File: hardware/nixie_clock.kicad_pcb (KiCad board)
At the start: 2 copper layers, 224 x 70 mm, 100 parts, among them J1 Conn_02x02_Odd_Even, J2 USB_C_Receptacle_USB2.0_16P, J7 Barrel_Jack_Switch, Q1 IRF740, Q2 BSS138, Q3 BSS138, Q4 BSS138, Q5 BSS138, Q6 BSS138, Q7 BSS138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

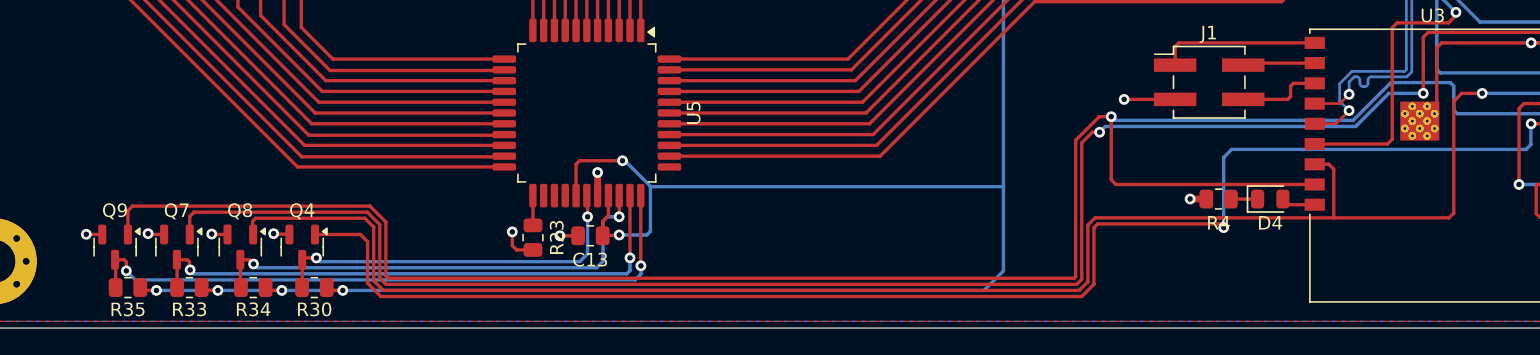
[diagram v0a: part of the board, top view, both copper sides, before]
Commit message: Remove one mosfet on the right since SPI out from the first HV5622 is already on 12v level.
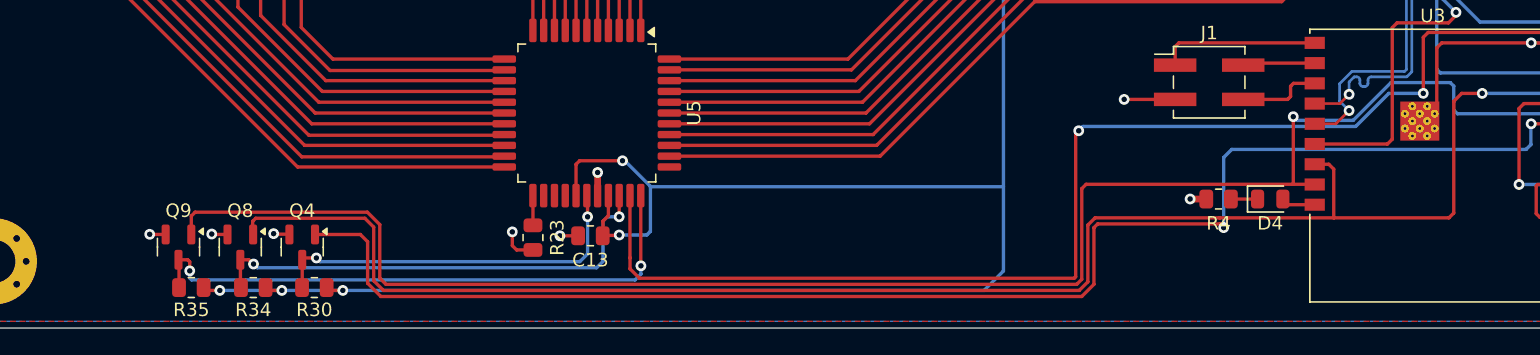
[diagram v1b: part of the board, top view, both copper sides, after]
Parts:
- removed Q7: BSS138, Package_TO_SOT_SMD:SOT-23
- removed R33: 10k, Resistor_SMD:R_0805_2012Metric
- moved Q9 4.70 mm to (68.7, 124.0)
- moved R35 4.70 mm to (69.6, 127.0)
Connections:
- U5 pad 32: Net-(Q7-D) -> /driver_3_digits_1_dot_left/SPI_SDO
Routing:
- net Net-(Q7-D): track 42.1 -> 0.00 mm, vias 2 -> 0
- net /driver_3_digits_1_dot_left/SPI_SDO: track 196.7 -> 163.8 mm
- net /cpu/GPIO1: track 246.2 -> 223.4 mm
- net /connectors/12V: track 462.0 -> 456.4 mm, vias 15 -> 14
- net Net-(Q9-D): track 48.1 -> 43.7 mm
- net /connectors/GND: track 135.9 -> 134.6 mm, vias 34 -> 33

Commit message: Tweaks.
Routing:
- net /connectors/12V: track 456.4 -> 427.4 mm
- net /connectors/GND: track 134.6 -> 133.8 mm

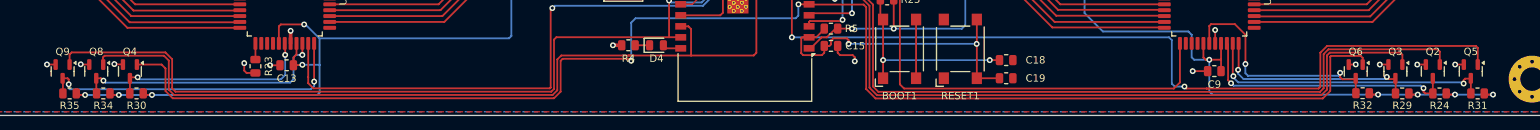
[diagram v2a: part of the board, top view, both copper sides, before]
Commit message: Making tracks to mosfets shorter.
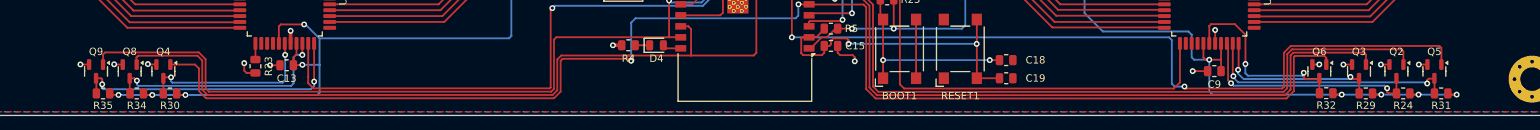
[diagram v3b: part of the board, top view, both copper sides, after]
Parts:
- moved Q2 4.96 mm to (250.5, 124.0)
- moved Q3 4.96 mm to (245.4, 124.0)
- moved Q6 4.96 mm to (240.0, 124.0)
- moved R29 4.96 mm to (246.3, 127.0)
- moved R32 4.96 mm to (240.9, 127.0)
- moved Q5 4.96 mm to (255.7, 124.0)
- moved R24 4.96 mm to (251.4, 127.0)
- moved R31 4.96 mm to (256.6, 127.0)
- moved Q4 4.56 mm to (82.4, 124.0)
- moved Q8 4.56 mm to (77.8, 124.0)
- moved Q9 4.56 mm to (73.3, 124.0)
- moved R30 4.56 mm to (83.3, 127.0)
- moved R34 4.56 mm to (78.8, 127.0)
- moved R35 4.56 mm to (74.2, 127.0)
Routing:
- net /cpu/SPI_CLK: track 200.9 -> 191.3 mm
- net /cpu/GPIO2: track 225.8 -> 216.3 mm
- net /cpu/GPIO1: track 223.4 -> 213.9 mm
- net Net-(Q6-D): track 31.4 -> 26.4 mm
- net Net-(Q5-D): track 40.0 -> 35.0 mm
- net Net-(Q3-D): track 28.2 -> 23.2 mm
- net Net-(Q2-D): track 36.1 -> 31.1 mm
- net /connectors/12V: track 427.4 -> 422.4 mm
- net /cpu/SPI_MOSI: track 115.6 -> 110.6 mm
- net Net-(Q9-D): track 43.7 -> 39.1 mm
- net Net-(Q8-D): track 35.4 -> 31.8 mm
- net Net-(Q4-D): track 28.1 -> 24.7 mm

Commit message: Update.
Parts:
- moved Q8 0.70 mm to (78.5, 124.0)
- moved Q9 0.70 mm to (74.0, 124.0)
- moved R30 0.70 mm to (84.0, 127.0)
- moved R34 0.70 mm to (79.5, 127.0)
- moved R35 0.70 mm to (74.9, 127.0)
- moved Q4 0.70 mm to (83.1, 124.0)
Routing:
- net /cpu/GPIO2: track 216.3 -> 215.6 mm
- net /cpu/GPIO1: track 213.9 -> 213.2 mm
- net Net-(Q9-D): track 39.1 -> 38.4 mm
- net Net-(Q4-D): track 24.7 -> 24.0 mm
- net Net-(Q8-D): track 31.8 -> 31.1 mm
- net /cpu/SPI_CLK: track 191.3 -> 190.6 mm

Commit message: Remove one via near HV5622. Tweaks.
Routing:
- net /connectors/GND: track 133.8 -> 131.1 mm, vias 33 -> 32
- net /connectors/12V: track 422.4 -> 423.6 mm
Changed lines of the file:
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@@
 	)
 	(segment
-		(start 191.7402 117.7198)
+		(start 191.7402 117.8098)
 		(end 191.7402 79.17)
 		(width 0.25)
@@
 	)
 	(segment
-		(start 176.305 118.17)
-		(end 176.3 118.165)
+		(start 181.984 118.17)
+		(end 191.38 118.17)
 		(width 0.25)
 		(layer "B.Cu")
@@
 	)
 	(segment
-		(start 181.984 118.17)
-		(end 191.29 118.17)
+		(start 191.38 118.17)
+		(end 191.7402 117.8098)
 		(width 0.25)
 		(layer "B.Cu")
@@
 	)
 	(segment
-		(start 181.984 118.17)
-		(end 176.305 118.17)
+		(start 176.305 118.17)
+		(end 176.3 118.165)
 		(width 0.25)
 		(layer "B.Cu")
@@
 	)
 	(segment
-		(start 191.29 118.17)
-		(end 191.7402 117.7198)
+		(start 181.984 118.17)
+		(end 176.305 118.17)
 		(width 0.25)
 		(layer "B.Cu")
@@
 	)
 	(segment
-		(start 207.3977 61.5275)
-		(end 207.9852 62.115)
+		(start 129.87 119.135)
+		(end 129.87 72.38)
 		(width 0.25)
 		(layer "B.Cu")
@@
 	)
 	(segment
-		(start 96.04 61.5275)
-		(end 207.4075 61.5275)
+		(start 207.3977 61.5275)
+		(end 207.9852 62.115)
 		(width 0.25)
 		(layer "B.Cu")
@@
 	)
 	(segment
-		(start 129.55 119.49)
-		(end 129.87 119.17)
+		(start 96.04 61.5275)
+		(end 207.4075 61.5275)
 		(width 0.25)
 		(layer "B.Cu")
@@
 	)
 	(segment
-		(start 103.69 119.49)
-		(end 129.55 119.49)
-		(width 0.25)
-		(layer "B.Cu")
-		(net 12)
-	)
-	(segment
 		(start 225.46 127.16)
 		(end 243.05 127.16)
@@
 	)
 	(segment
-		(start 103.72 126.9)
-		(end 103.72 123.11)
+		(start 207.995 76.035033)
+		(end 207.995 118.2025)
 		(width 0.25)
 		(layer "B.Cu")
@@
 	)
 	(segment
-		(start 207.995 116.05)
-		(end 210.5 118.555)
+		(start 103.72 126.9)
+		(end 103.72 123.11)
 		(width 0.25)
 		(layer "B.Cu")
@@
 	)
 	(segment
-		(start 222.15 118.555)
-		(end 222.6 119.005)
+		(start 208.3475 118.555)
+		(end 222.15 118.555)
 		(width 0.25)
 		(layer "B.Cu")
@@
 	)
 	(segment
-		(start 129.87 119.17)
-		(end 129.87 72.38)
+		(start 101.62 117.595)
+		(end 101.795 117.595)
 		(width 0.25)
 		(layer "B.Cu")
@@
 	)
 	(segment
-		(start 222.6 122.075)
-		(end 222.93 122.405)
+		(start 96.039792 61.527708)
+		(end 96.04 61.5275)
 		(width 0.25)
 		(layer "B.Cu")
@@
 	)
 	(segment
-		(start 96.039792 61.527708)
-		(end 96.04 61.5275)
+		(start 88.6575 61.5275)
+		(end 88.399792 61.785208)
 		(width 0.25)
 		(layer "B.Cu")
@@
 	)
 	(segment
-		(start 88.6575 61.5275)
-		(end 88.399792 61.785208)
+		(start 101.795 117.595)
+		(end 103.69 119.49)
 		(width 0.25)
 		(layer "B.Cu")
@@
 	)
 	(segment
-		(start 210.5 118.555)
-		(end 222.15 118.555)
+		(start 129.515 119.49)
+		(end 129.87 119.135)
 		(width 0.25)
 		(layer "B.Cu")
@@
 	)
 	(segment
-		(start 101.795 117.595)
-		(end 103.69 119.49)
+		(start 103.69 119.49)
+		(end 129.515 119.49)
 		(width 0.25)
 		(layer "B.Cu")
@@
 	)
 	(segment
+		(start 222.6 122.075)
+		(end 222.93 122.405)
+		(width 0.25)
+		(layer "B.Cu")
+		(net 12)
+	)
+	(segment
 		(start 101.375 123.1)
 		(end 103.71 123.1)
@@
 	)
 	(segment
-		(start 222.6 119.005)
-		(end 222.6 122.075)
+		(start 222.15 118.555)
+		(end 222.6 119.005)
 		(width 0.25)
 		(layer "B.Cu")
@@
 	)
 	(segment
-		(start 258.72 127.16)
-		(end 253.52 127.16)
+		(start 222.93 122.405)
+		(end 225 122.405)
 		(width 0.25)
 		(layer "B.Cu")
@@
 	)
 	(segment
-		(start 222.93 122.405)
-		(end 225 122.405)
+		(start 207.995 118.2025)
+		(end 208.3475 118.555)
 		(width 0.25)
 		(layer "B.Cu")
@@
 	)
 	(segment
-		(start 207.9852 62.115)
-		(end 207.9852 76.035033)
+		(start 258.72 127.16)
+		(end 253.52 127.16)
 		(width 0.25)
 		(layer "B.Cu")
@@
 	)
 	(segment
-		(start 101.62 117.595)
-		(end 101.795 117.595)
+		(start 207.9852 62.115)
+		(end 207.9852 76.035033)
 		(width 0.25)
 		(layer "B.Cu")
@@
 	)
 	(segment
-		(start 207.995 76.035033)
-		(end 207.995 116.05)
+		(start 222.6 119.005)
+		(end 222.6 122.075)
 		(width 0.25)
 		(layer "B.Cu")
@@
 	)
 	(segment
-		(start 93.45 122.87)
-		(end 93.45 123.89)
-		(width 0.25)
-		(layer "F.Cu")
-		(net 122)
-	)
-	(segment
 		(start 97.669792 71.0075)
 		(end 96.072292 71.0075)
@@
 	)
 	(segment
-		(start 93.45 123.89)
-		(end 93.7675 124.2075)
-		(width 0.25)
-		(layer "F.Cu")
-		(net 122)
-	)
-	(segment
 		(start 126.27 73.75)
 		(end 126.28 73.74)
@@
 	)
 	(segment
-		(start 93.7675 124.2075)
-		(end 94.98 124.2075)
-		(width 0.25)
-		(layer "F.Cu")
-		(net 122)
-	)
-	(segment
 		(start 198.324 122.3625)
 		(end 198.2265 122.46)
@@
 		(size 0.8)
 		(drill 0.4)
-		(layers "F.Cu" "B.Cu")
-		(net 122)
-	)
-	(via
-		(at 93.45 122.87)
-		(size 0.8)
-		(drill 0.4)

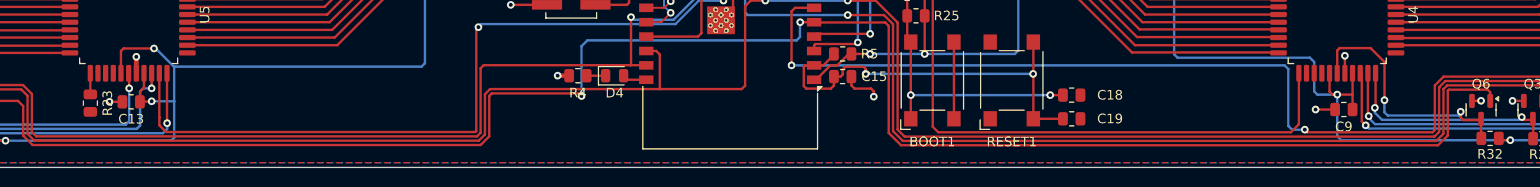
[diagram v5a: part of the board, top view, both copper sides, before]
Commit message: Remove one unused track.
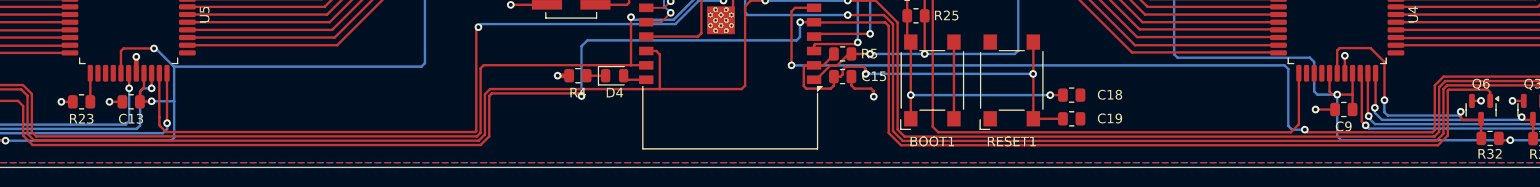
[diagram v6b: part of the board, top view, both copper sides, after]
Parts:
- moved R23 0.92 mm to (94.1, 123.2), turned to 180 degrees
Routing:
- net /connectors/GND: track 131.1 -> 132.3 mm, vias 32 -> 33
- net Net-(U5A-DATA_OUT): track 2.20 -> 2.98 mm
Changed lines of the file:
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@@
 	(footprint "Resistor_SMD:R_0805_2012Metric"
 		(layer "F.Cu")
-		(at 94.98 123.295 -90)
+		(at 94.07 123.16 180)
 		(descr "Resistor SMD 0805 (2012 Metric), square (rectangular) end terminal, IPC-7351 nominal, (Body size source: IPC-SM-782 page 72, https://www.pcb-3d.com/wordpress/wp-content/uploads/ipc-sm-782a_amendment_1_and_2.pdf), generated with kicad-footprint-generator")
 		(tags "resistor")
 		(property "Reference" "R23"
-			(at 0 -1.8 90)
+			(at 0 -1.8 0)
 			(layer "F.SilkS")
 			(effects
@@
 		)
 		(property "Value" "10K"
-			(at 0 2.42 90)
+			(at 0 2.42 0)
 			(layer "F.Fab")
 			(effects
@@
 		)
 		(property "Datasheet" ""
-			(at 0 0 90)
+			(at 0 0 0)
 			(layer "F.Fab")
 			(hide yes)
@@
 		)
 		(property "Description" "Resistor"
-			(at 0 0 90)
+			(at 0 0 0)
 			(layer "F.Fab")
 			(hide yes)
@@
 		)
 		(fp_line
-			(start -1.68 0.95)
-			(end -1.68 -0.95)
+			(start 1.68 0.95)
+			(end -1.68 0.95)
 			(stroke
 				(width 0.05)
@@
 		)
 		(fp_line
-			(start 1.68 0.95)
-			(end -1.68 0.95)
+			(start 1.68 -0.95)
+			(end 1.68 0.95)
 			(stroke
 				(width 0.05)
@@
 		)
 		(fp_line
-			(start -1.68 -0.95)
-			(end 1.68 -0.95)
+			(start -1.68 0.95)
+			(end -1.68 -0.95)
 			(stroke
 				(width 0.05)
@@
 		)
 		(fp_line
-			(start 1.68 -0.95)
-			(end 1.68 0.95)
+			(start -1.68 -0.95)
+			(end 1.68 -0.95)
 			(stroke
 				(width 0.05)
@@
 		)
 		(fp_line
-			(start -1 0.625)
-			(end -1 -0.625)
+			(start 1 0.625)
+			(end -1 0.625)
 			(stroke
 				(width 0.1)
@@
 		)
 		(fp_line
-			(start 1 0.625)
-			(end -1 0.625)
+			(start 1 -0.625)
+			(end 1 0.625)
 			(stroke
 				(width 0.1)
@@
 		)
 		(fp_line
-			(start -1 -0.625)
-			(end 1 -0.625)
+			(start -1 0.625)
+			(end -1 -0.625)
 			(stroke
 				(width 0.1)
@@
 		)
 		(fp_line
-			(start 1 -0.625)
-			(end 1 0.625)
+			(start -1 -0.625)
+			(end 1 -0.625)
 			(stroke
 				(width 0.1)
@@
 		)
 		(fp_text user "${REFERENCE}"
-			(at 0 0 90)
+			(at 0 0 0)
 			(layer "F.Fab")
 			(effects
@@
 		)
 		(pad "1" smd roundrect
-			(at -0.9125 0 270)
+			(at -0.9125 0 180)
 			(size 1.025 1.4)
 			(layers "F.Cu" "F.Mask" "F.Paste")
@@
 		)
 		(pad "2" smd roundrect
-			(at 0.9125 0 270)
+			(at 0.9125 0 180)
 			(size 1.025 1.4)
 			(layers "F.Cu" "F.Mask" "F.Paste")
@@
 	)
 	(segment
-		(start 94.98 120.185)
-		(end 94.975 120.18)
+		(start 94.9825 123.16)
+		(end 94.9825 120.1875)
 		(width 0.25)
 		(layer "F.Cu")
@@
 	)
 	(segment
-		(start 94.98 122.3825)
-		(end 94.98 120.185)
+		(start 94.9825 120.1875)
+		(end 94.975 120.18)
 		(width 0.25)
 		(layer "F.Cu")
@@
 	)
 	(segment
+		(start 93.1575 123.16)
+		(end 91.94 123.16)
+		(width 0.25)
+		(layer "F.Cu")
+		(net 122)
+	)
+	(segment
 		(start 96.069792 71.01)
 		(end 96.072292 71.0075)
@@
 	)
 	(segment
-		(start 240.02 123.05)
-		(end 240.01 123.06)
-		(width 0.25)
-		(layer "F.Cu")
-		(net 122)
-	)
-	(segment
 		(start 249.56 123.0625)
 		(end 248.45 123.0625)
@@
 		(size 0.8)
 		(drill 0.4)
+		(layers "F.Cu" "B.Cu")
+		(net 122)
+	)
+	(via
+		(at 91.96 123.16)
+		(size 0.8)
+		(drill 0.4)

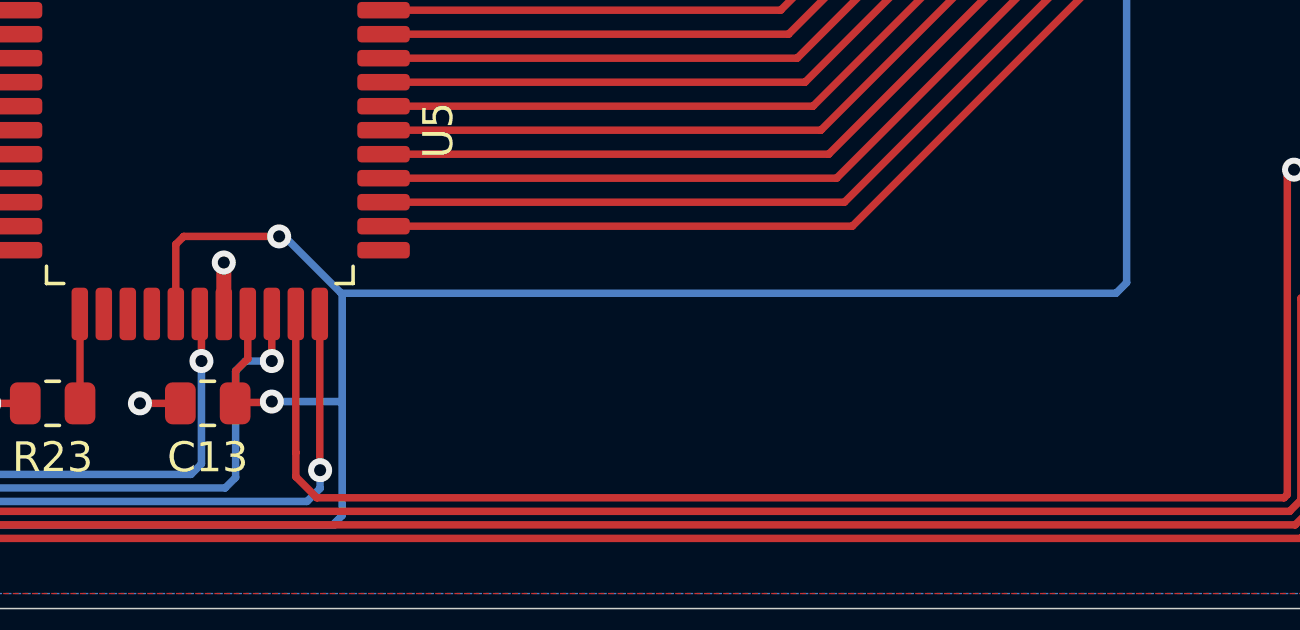
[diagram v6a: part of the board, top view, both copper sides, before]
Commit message: Simplify 12V rail on U5.
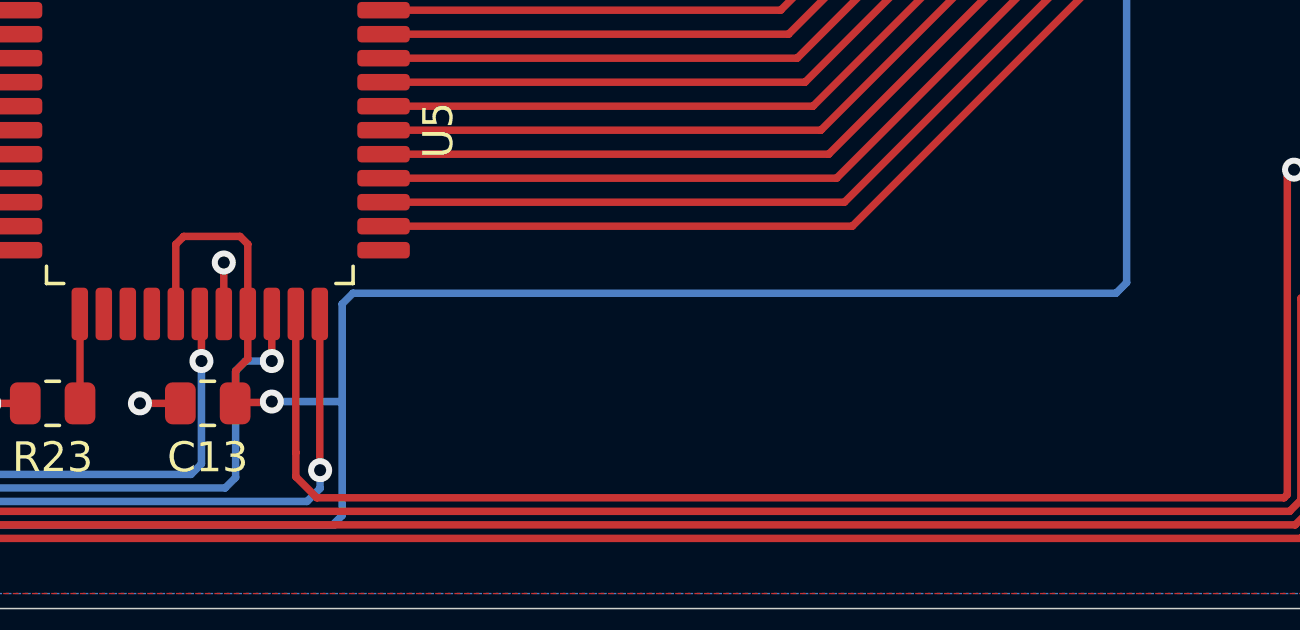
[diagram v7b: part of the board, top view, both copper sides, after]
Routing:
- net /connectors/12V: track 423.6 -> 422.0 mm, vias 14 -> 13
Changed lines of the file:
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@@
 	)
 	(segment
+		(start 100.315 117.595)
+		(end 98.44 117.595)
+		(width 0.25)
+		(layer "F.Cu")
+		(net 12)
+	)
+	(segment
+		(start 100.575 120.18)
+		(end 100.575 117.855)
+		(width 0.25)
+		(layer "F.Cu")
+		(net 12)
+	)
+	(segment
 		(start 81.62 127.21)
 		(end 80.5525 127.21)
@@
 	)
 	(segment
-		(start 131.1375 74.01)
-		(end 130.15 74.01)
+		(start 98.44 117.595)
+		(end 98.175 117.86)
 		(width 0.25)
 		(layer "F.Cu")
@@
 	)
 	(segment
-		(start 101.62 117.595)
-		(end 98.44 117.595)
+		(start 131.1375 74.01)
+		(end 130.15 74.01)
 		(width 0.25)
 		(layer "F.Cu")
@@
 	)
 	(segment
-		(start 98.175 117.86)
-		(end 98.175 120.18)
+		(start 224.505 122.405)
+		(end 224.2 122.1)
 		(width 0.25)
 		(layer "F.Cu")
@@
 	)
 	(segment
-		(start 224.505 122.405)
-		(end 224.2 122.1)
+		(start 226.6025 120.1825)
+		(end 226.6 120.18)
 		(width 0.25)
 		(layer "F.Cu")
@@
 	)
 	(segment
-		(start 226.6025 120.1825)
-		(end 226.6 120.18)
+		(start 100.575 117.855)
+		(end 100.315 117.595)
 		(width 0.25)
 		(layer "F.Cu")
@@
 	)
 	(segment
-		(start 98.44 117.595)
-		(end 98.175 117.86)
-		(width 0.25)
-		(layer "F.Cu")
-		(net 12)
-	)
-	(segment
 		(start 226.6025 123.84)
 		(end 226.6025 122.4)
@@
 	)
 	(segment
+		(start 98.175 117.86)
+		(end 98.175 120.18)
+		(width 0.25)
+		(layer "F.Cu")
+		(net 12)
+	)
+	(segment
 		(start 257.6825 127.16)
 		(end 257.5225 127)
@@
 	)
 	(via
-		(at 101.62 117.595)
-		(size 0.8)
-		(drill 0.4)
-		(layers "F.Cu" "B.Cu")
-		(net 12)
-	)
-	(via
 		(at 225 122.405)
 		(size 0.8)
@@
 	)
 	(segment
-		(start 129.87 119.135)
-		(end 129.87 72.38)
-		(width 0.25)
-		(layer "B.Cu")
-		(net 12)
-	)
-	(segment
 		(start 207.3977 61.5275)
 		(end 207.9852 62.115)
@@
 	)
 	(segment
-		(start 96.04 61.5275)
-		(end 207.4075 61.5275)
+		(start 104.08 119.49)
+		(end 129.515 119.49)
 		(width 0.25)
 		(layer "B.Cu")
@@
 	)
 	(segment
-		(start 103.72 123.11)
-		(end 103.72 119.55)
+		(start 96.04 61.5275)
+		(end 207.4075 61.5275)
 		(width 0.25)
 		(layer "B.Cu")
@@
 	)
 	(segment
+		(start 129.515 119.49)
+		(end 129.87 119.135)
+		(width 0.25)
+		(layer "B.Cu")
+		(net 12)
+	)
+	(segment
 		(start 103.72 126.9)
 		(end 103.72 123.11)
@@
 	)
 	(segment
+		(start 129.87 119.135)
+		(end 129.87 72.38)
+		(width 0.25)
+		(layer "B.Cu")
+		(net 12)
+	)
+	(segment
 		(start 208.3475 118.555)
 		(end 222.15 118.555)
@@
 	)
 	(segment
-		(start 101.62 117.595)
-		(end 101.795 117.595)
-		(width 0.25)
-		(layer "B.Cu")
-		(net 12)
-	)
-	(segment
 		(start 96.039792 61.527708)
 		(end 96.04 61.5275)
@@
 	)
 	(segment
-		(start 101.795 117.595)
-		(end 103.69 119.49)
+		(start 103.72 123.11)
+		(end 103.72 119.85)
 		(width 0.25)
 		(layer "B.Cu")
@@
 	)
 	(segment
-		(start 129.515 119.49)
-		(end 129.87 119.135)
-		(width 0.25)
-		(layer "B.Cu")
-		(net 12)
-	)
-	(segment
 		(start 225 126.74)
 		(end 225.42 127.16)
@@
 	)
 	(segment
-		(start 103.69 119.49)
-		(end 129.515 119.49)
-		(width 0.25)
-		(layer "B.Cu")
-		(net 12)
-	)
-	(segment
 		(start 103.5 127.21)
 		(end 80.97 127.21)
@@
 	)
 	(segment
+		(start 103.72 119.85)
+		(end 104.08 119.49)
+		(width 0.25)
+		(layer "B.Cu")
+		(net 12)
+	)
+	(segment
 		(start 248.45 127.16)
 		(end 243.05 127.16)
@@
 		(start 99.775 118.465)
 		(end 99.775 120.18)
-		(width 0.5)
+		(width 0.25)
 		(layer "F.Cu")
 		(net 122)
